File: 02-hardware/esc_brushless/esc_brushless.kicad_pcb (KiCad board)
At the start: 4 copper layers, 64.6 x 29.8 mm, 98 parts, among them J1 Conn_HE13_1x1_5.08V, J2 Conn_HE13_1x1_5.08V, J4 DNP, J5 Conn_HE13_1x2_2.54V, J6 DNP, J7 DNP, J8 DNP, Q1 IPD30N03S4L_09, Q2 IPD30N03S4L_09, Q3 IPD30N03S4L_09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

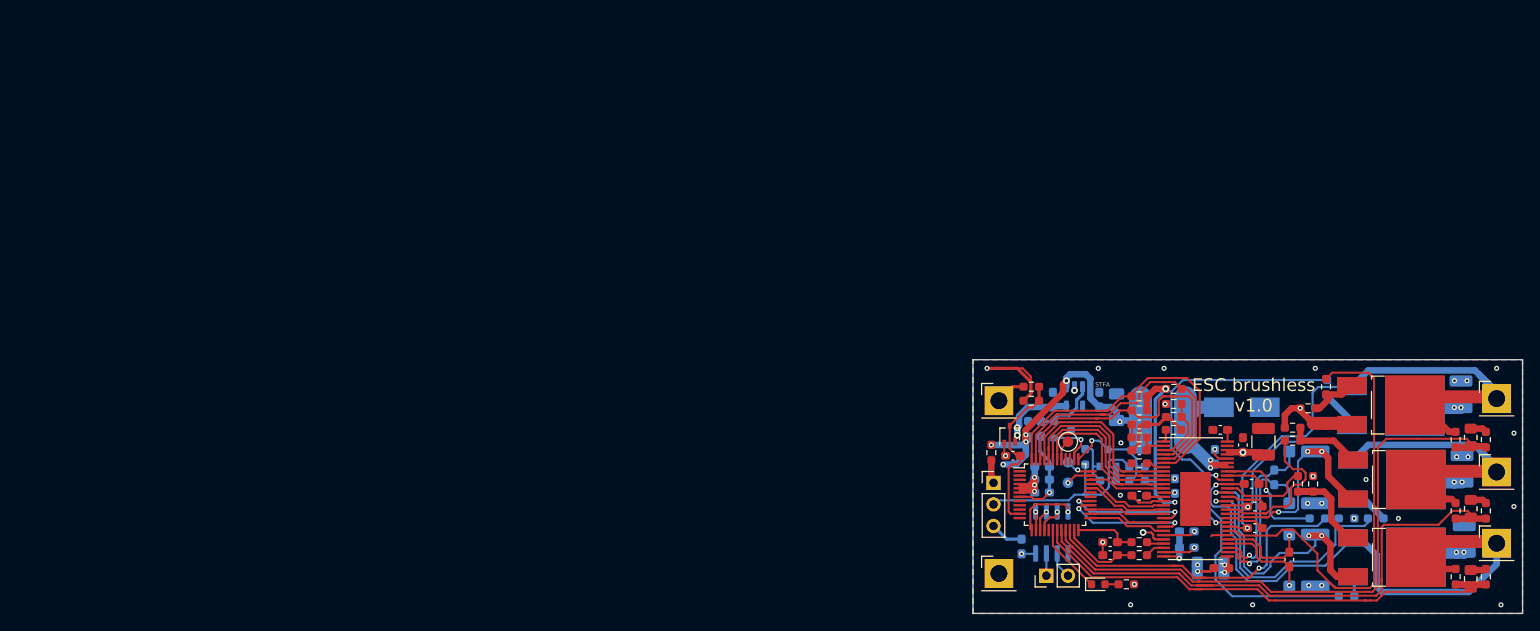
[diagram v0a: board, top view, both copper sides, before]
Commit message: Schematic and PCB v1.1.0 - Converted to KiCAD6, all DRC cleared
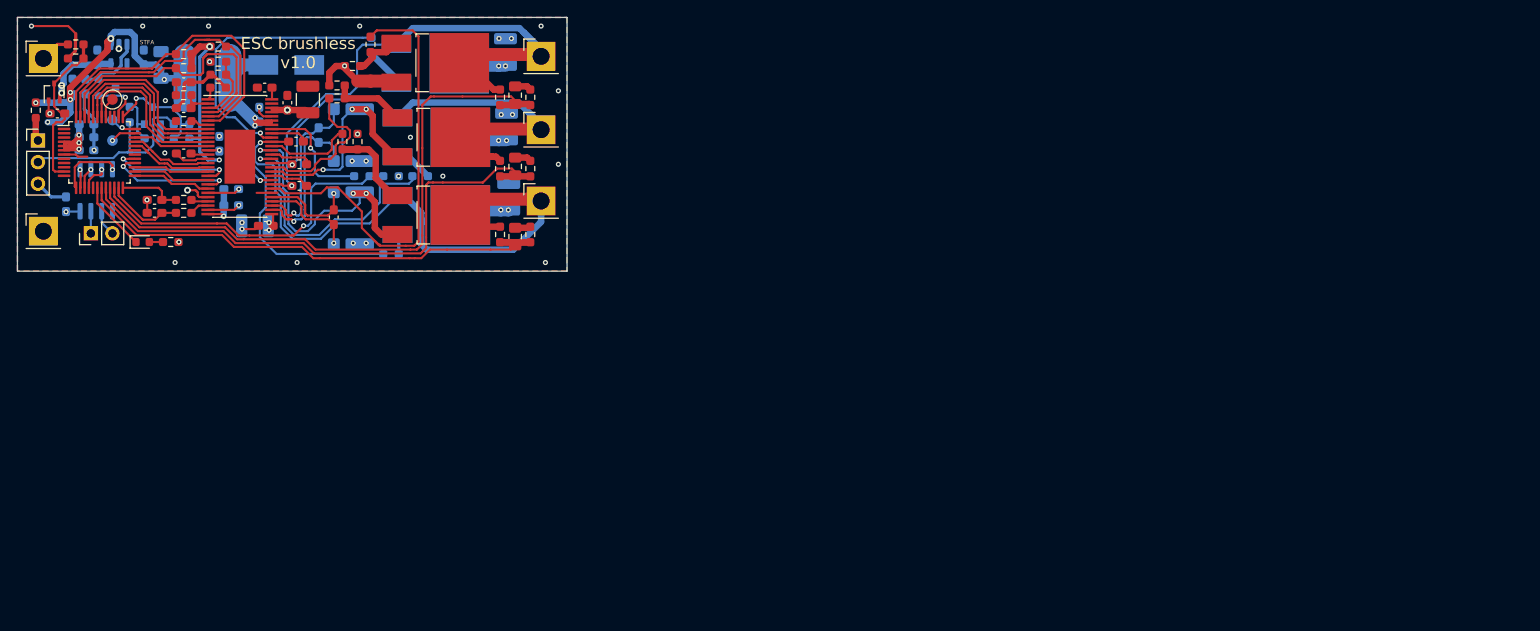
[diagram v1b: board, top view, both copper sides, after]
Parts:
- C10, C9: value 47u -> 4.7u
- C11, C12: value 4.7u -> 0.1u
- C13, C14: value 1u -> 2.2n
- C17: value 4.7u -> 15n
- C25: value 4.7u -> 6.8n
- C26: value 4.7u -> 39p
- C3, C4, C5: value C_1210 -> 2.2u
- C30: value C_0603 -> 2.2u
- C33: value C_0603 -> 1u
- L1: value 22u -> 33u
- Q1, Q2, Q3, Q4, Q5, Q6: value IPD30N03S4L_09 -> IPD70N03S4L04ATMA1
- R15, R16, R17, R38, R41, R44, R5: value R_0603 -> 10k
- R20, R22, R24: value R_0603 -> 43k
- R21, R23, R25: value R_0603 -> 4.7k
- R29, R30: value 10k -> 56
- R32: value 10k -> 205k
- R33: value 10k -> 53.6k
- R35: value 10k -> 28k
- R40, R42: value R_0603 -> 100k
- R43: value R_0603 -> 47k
- R6: value R_CTN_0608 -> 10k@25°c
- TP1, TP2, TP3: value test_point -> test_point_smd
- moved C13 119.4 mm to (93.0, 72.3)
- moved C14 119.4 mm to (93.0, 73.8)
- moved C15 119.4 mm to (102.0, 71.0)
- moved C16 119.4 mm to (102.0, 72.9)
- moved C18 119.4 mm to (109.6, 65.4)
- moved C19 119.4 mm to (110.0, 68.1)
- moved C2 119.4 mm to (112.3, 64.6)
- moved C20 119.4 mm to (110.0, 70.6)
- moved C22 119.4 mm to (96.4, 66.8)
- moved C23 119.4 mm to (100.6, 65.7)
- moved C24 119.4 mm to (93.7, 56.4)
- moved C25 119.4 mm to (96.4, 58.4)
- moved C26 119.4 mm to (96.4, 61.5)
- moved C27 119.4 mm to (85.0, 63.4)
- moved C28 119.4 mm to (85.0, 66.4)
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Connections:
- net +3V3 renamed +3.3V
- net /RS488_phy/RS485_DE renamed /microcontroller/RS485_DE
- net /RS488_phy/RS485_RX renamed /microcontroller/UART_RX
- net /RS488_phy/RS485_TX renamed /microcontroller/UART_TX
- net /RS488_phy/\RS485_RE renamed /microcontroller/\RS485_RE
- net /mos drive stage/SPI_CLK renamed /microcontroller/SPI_SCK
- net /mos power stage/MOTOR_PH1 renamed /mos drive stage/SH_A
- net /mos power stage/MOTOR_PH2 renamed /mos drive stage/SH_B
- net /mos power stage/MOTOR_PH3 renamed /mos drive stage/SH_C
- U1 pad 55: Net-(U1-Pad55) -> unconnected-(U1-Pad55)
- U2 pad 1: Net-(U2-Pad1) -> unconnected-(U2-Pad1)
- U2 pad 10: Net-(U2-Pad10) -> unconnected-(U2-Pad10)
- U2 pad 12: Net-(U2-Pad12) -> unconnected-(U2-Pad12)
- U2 pad 17: Net-(U2-Pad17) -> unconnected-(U2-Pad17)
- U2 pad 2: Net-(U2-Pad2) -> unconnected-(U2-Pad2)
- U2 pad 3: Net-(U2-Pad3) -> unconnected-(U2-Pad3)
- U2 pad 30: Net-(U2-Pad30) -> unconnected-(U2-Pad30)
- U2 pad 31: Net-(U2-Pad31) -> unconnected-(U2-Pad31)
- U2 pad 39: Net-(U2-Pad39) -> unconnected-(U2-Pad39)
- U2 pad 40: Net-(U2-Pad40) -> unconnected-(U2-Pad40)
- U2 pad 8: Net-(U2-Pad8) -> unconnected-(U2-Pad8)
- U2 pad 9: Net-(U2-Pad9) -> unconnected-(U2-Pad9)
- U3 pad 4: Net-(U3-Pad4) -> unconnected-(U3-Pad4)
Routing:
- net GND: track 73.7 -> 63.7 mm
- net /mos drive stage/SH_C: track 74.9 -> 68.3 mm
- net /mos drive stage/V_PWR: track 33.6 -> 29.5 mm
- net /mos drive stage/SH_A: track 78.8 -> 76.1 mm
- net /microcontroller/ADC_B: track 67.5 -> 64.8 mm
- net Net-(C30-Pad1): track 12.2 -> 10.5 mm
- net /microcontroller/ADC_A: track 62.7 -> 61.2 mm
- net /microcontroller/SPI_SCK: track 20.8 -> 19.5 mm
- net /SENSOR_1: track 41.0 -> 39.8 mm
- net /microcontroller/SPI_MISO: track 21.3 -> 20.3 mm
- net +3.3V: track 130.7 -> 129.7 mm
- net /microcontroller/SPI_MOSI: track 22.0 -> 21.0 mm
- net /microcontroller/PWM: track 14.1 -> 13.3 mm
- net /mos drive stage/GH_C: track 39.2 -> 38.4 mm
- net /microcontroller/ADC_C: track 73.4 -> 72.7 mm
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- added copper zone on In2.Cu, net /mos drive stage/V_PWR
- added copper zone on In1.Cu, net GND
- removed copper zone on Power, net /mos drive stage/V_PWR
- removed copper zone on GND, net GND
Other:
- net class Default removed
- net class JLCPCB removed
